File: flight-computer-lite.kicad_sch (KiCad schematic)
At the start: 44 parts, among them J1 USB_C_Receptacle_USB2.0_16P, J2 Micro_SD_Card_Det2, J3 Conn_01x02_Pin, J4 Conn_01x03_Pin, Q1 BSS138, SW1 SW_Push, SW2 SW_Push, U1 RP2040, U2 W25Q32JVZP, Y1 SiT1602BI-22-33E-12.000000E

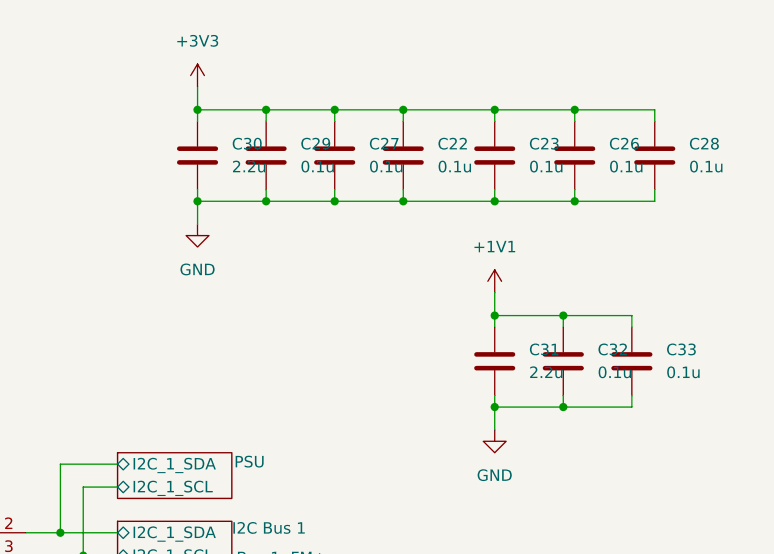
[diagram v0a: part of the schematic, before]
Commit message: Adjusted VREG IN/OUT Decoupling capacitor values to match datasheet suggestion
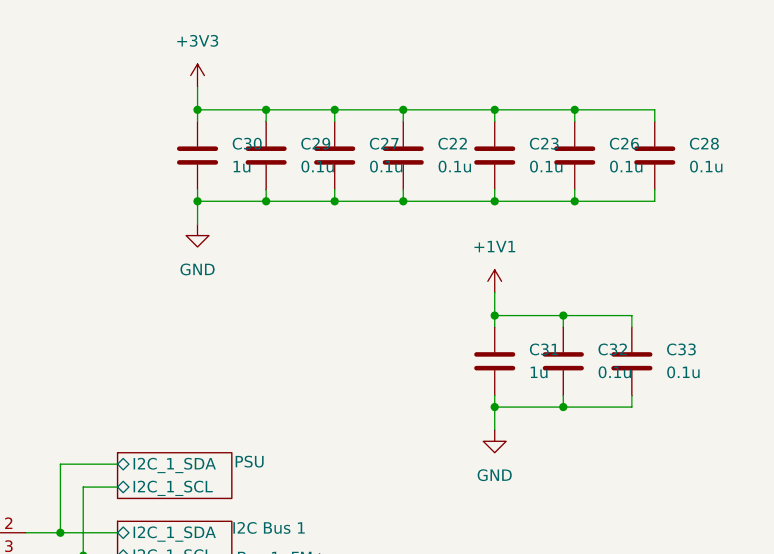
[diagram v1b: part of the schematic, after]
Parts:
- C30, C31: value 2.2u -> 1u
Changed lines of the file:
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@@
 			)
 		)
-		(property "Value" "2.2u"
+		(property "Value" "1u"
 			(at 255.27 54.6099 0)
 			(effects
@@
 			)
 		)
-		(property "Value" "2.2u"
+		(property "Value" "1u"
 			(at 222.25 31.7499 0)
 			(effects

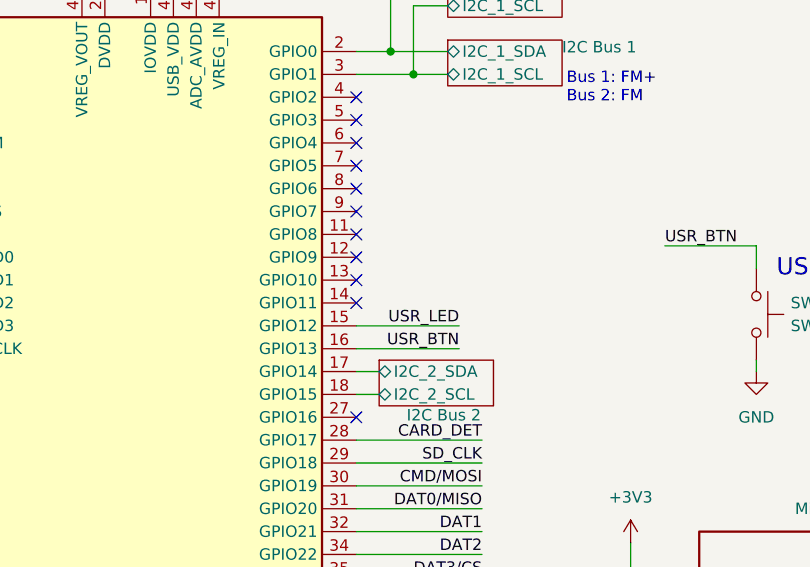
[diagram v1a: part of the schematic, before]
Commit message: Changed USR_LED and USR_BTN pins
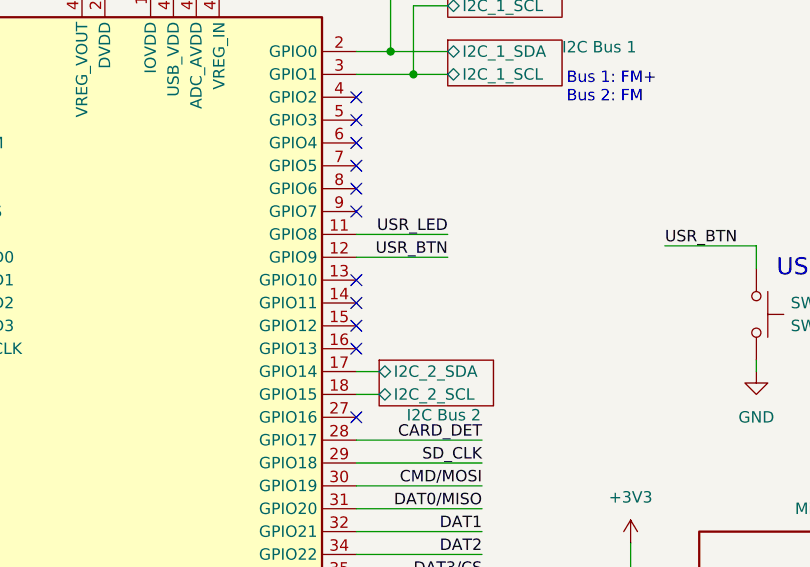
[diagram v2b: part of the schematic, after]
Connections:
- net USR_BTN: now also U1.12 (GPIO9); no longer U1.16 (GPIO13)
- net USR_LED: now also U1.11 (GPIO8); no longer U1.15 (GPIO12)
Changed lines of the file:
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@@
-	)
-	(no_connect
-		(at 199.39 95.25)
-	)
-	(no_connect
-		(at 199.39 92.71)
 	)
 	(no_connect
@@
 	)
 	(no_connect
+		(at 199.39 105.41)
+	)
+	(no_connect
 		(at 199.39 85.09)
 	)
@@
 	)
 	(no_connect
+		(at 199.39 102.87)
+	)
+	(no_connect
 		(at 199.39 100.33)
 	)
@@
 	(wire
 		(pts
+			(xy 199.39 92.71) (xy 209.55 92.71)
+		)
+		(stroke
+			(width 0)
+			(type default)
+		)
+	)
+	(wire
+		(pts
 			(xy 251.46 49.53) (xy 251.46 48.26)
 		)
@@
 	(wire
 		(pts
-			(xy 199.39 105.41) (xy 210.82 105.41)
-		)
-		(stroke
-			(width 0)
-			(type default)
-		)
-	)
-	(wire
-		(pts
 			(xy 205.74 67.31) (xy 205.74 74.93)
 		)
@@
 	(wire
 		(pts
+			(xy 199.39 95.25) (xy 209.55 95.25)
+		)
+		(stroke
+			(width 0)
+			(type default)
+		)
+	)
+	(wire
+		(pts
 			(xy 78.74 163.83) (xy 82.55 163.83)
 		)
@@
 		(pts
 			(xy 179.07 64.77) (xy 179.07 63.5)
-		)
-		(stroke
-			(width 0)
-			(type default)
-		)
-	)
-	(wire
-		(pts
-			(xy 199.39 102.87) (xy 210.82 102.87)
 		)
 		(stroke
@@
 	)
 	(label "USR_BTN"
-		(at 210.82 105.41 180)
+		(at 209.55 95.25 180)
 		(fields_autoplaced yes)
 		(effects
@@
 	)
 	(label "USR_LED"
-		(at 210.82 102.87 180)
-		(fields_autoplaced yes)
-		(effects
+		(at 209.55 92.71 180)
+		(fields_autoplaced yes)
+		(effects

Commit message: oops wrong pin again
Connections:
- net USR_BTN: now also U1.9 (GPIO7); no longer U1.12 (GPIO9)
- net USR_LED: now also U1.8 (GPIO6); no longer U1.11 (GPIO8)
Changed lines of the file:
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@@
+	)
+	(no_connect
+		(at 199.39 95.25)
+	)
+	(no_connect
+		(at 199.39 92.71)
 	)
 	(no_connect
@@
 	)
 	(no_connect
-		(at 199.39 87.63)
-	)
-	(no_connect
 		(at 52.07 107.95)
 	)
@@
 		(at 199.39 80.01)
 	)
-	(no_connect
-		(at 199.39 90.17)
-	)
 	(wire
 		(pts
@@
 	(wire
 		(pts
-			(xy 199.39 92.71) (xy 209.55 92.71)
-		)
-		(stroke
-			(width 0)
-			(type default)
-		)
-	)
-	(wire
-		(pts
 			(xy 251.46 49.53) (xy 251.46 48.26)
 		)
@@
 	(wire
 		(pts
+			(xy 199.39 90.17) (xy 209.55 90.17)
+		)
+		(stroke
+			(width 0)
+			(type default)
+		)
+	)
+	(wire
+		(pts
 			(xy 81.28 31.75) (xy 78.74 31.75)
 		)
@@
 	(wire
 		(pts
+			(xy 199.39 87.63) (xy 209.55 87.63)
+		)
+		(stroke
+			(width 0)
+			(type default)
+		)
+	)
+	(wire
+		(pts
 			(xy 270.51 83.82) (xy 270.51 85.09)
 		)
@@
 		(pts
 			(xy 78.74 44.45) (xy 78.74 45.72)
-		)
-		(stroke
-			(width 0)
-			(type default)
-		)
-	)
-	(wire
-		(pts
-			(xy 199.39 95.25) (xy 209.55 95.25)
 		)
 		(stroke
@@
 	)
 	(label "USR_BTN"
-		(at 209.55 95.25 180)
+		(at 209.55 90.17 180)
 		(fields_autoplaced yes)
 		(effects
@@
 	)
 	(label "USR_LED"
-		(at 209.55 92.71 180)
-		(fields_autoplaced yes)
-		(effects
+		(at 209.55 87.63 180)
+		(fields_autoplaced yes)
+		(effects

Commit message: WIP layout/route
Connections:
- net BUZZER_CTL: now also U1.7 (GPIO5)
- net I2C Bus 2/I2C_2_SCL: now also U1.14 (GPIO11); no longer U1.18 (GPIO15)
- net I2C Bus 2/I2C_2_SDA: now also U1.13 (GPIO10); no longer U1.17 (GPIO14)
- no-connect marks 18 -> 17
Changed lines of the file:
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@@
 	)
 	(no_connect
+		(at 199.39 110.49)
+	)
+	(no_connect
 		(at 199.39 95.25)
 	)
@@
 	)
 	(no_connect
-		(at 199.39 97.79)
+		(at 199.39 107.95)
 	)
 	(no_connect
@@
 	)
 	(no_connect
-		(at 199.39 85.09)
-	)
-	(no_connect
 		(at 199.39 135.89)
 	)
@@
 	)
 	(no_connect
-		(at 199.39 100.33)
-	)
-	(no_connect
 		(at 199.39 133.35)
 	)
@@
 	(wire
 		(pts
-			(xy 199.39 110.49) (xy 201.93 110.49)
-		)
-		(stroke
-			(width 0)
-			(type default)
-		)
-	)
-	(wire
-		(pts
 			(xy 199.39 118.11) (xy 213.36 118.11)
 		)
@@
 	(wire
 		(pts
+			(xy 199.39 100.33) (xy 201.93 100.33)
+		)
+		(stroke
+			(width 0)
+			(type default)
+		)
+	)
+	(wire
+		(pts
 			(xy 218.44 25.4) (xy 226.06 25.4)
 		)
@@
 	(wire
 		(pts
+			(xy 199.39 85.09) (xy 213.36 85.09)
+		)
+		(stroke
+			(width 0)
+			(type default)
+		)
+	)
+	(wire
+		(pts
 			(xy 146.05 148.59) (xy 148.59 148.59)
 		)
@@
 	(wire
 		(pts
-			(xy 199.39 107.95) (xy 201.93 107.95)
-		)
-		(stroke
-			(width 0)
-			(type default)
-		)
-	)
-	(wire
-		(pts
 			(xy 132.08 80.01) (xy 148.59 80.01)
 		)
@@
 	(wire
 		(pts
+			(xy 199.39 97.79) (xy 201.93 97.79)
+		)
+		(stroke
+			(width 0)
+			(type default)
+		)
+	)
+	(wire
+		(pts
 			(xy 137.16 102.87) (xy 148.59 102.87)
 		)
@@
 		)
 	)
+	(label "BUZZER_CTL"
+		(at 213.36 85.09 180)
+		(fields_autoplaced yes)
+		(effects
+			(font
+				(size 1.27 1.27)
+			)
+			(justify right bottom)
+		)
+	)
 	(label "QSPI_SD3"
 		(at 57.15 44.45 180)
@@
 	)
 	(sheet
-		(at 201.93 106.68)
+		(at 201.93 96.52)
 		(size 12.7 5.08)
 		(stroke
@@
 		)
 		(property "Sheetname" "I2C Bus 2"
-			(at 204.978 113.538 0)
+			(at 204.978 103.632 0)
 			(effects
 				(font
@@
 		)
 		(property "Sheetfile" "I2C_Bus_2.kicad_sch"
-			(at 201.93 111.0746 0)
+			(at 201.93 100.9146 0)
 			(effects
 				(font
@@
 		)
 		(pin "I2C_2_SCL" bidirectional
-			(at 201.93 110.49 180)
+			(at 201.93 100.33 180)
 			(effects
 				(font
@@
 		)
 		(pin "I2C_2_SDA" bidirectional
-			(at 201.93 107.95 180)
+			(at 201.93 97.79 180)
 			(effects
 				(font

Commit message: major routing update!
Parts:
- R11: value 1k -> 1K
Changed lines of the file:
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@@
 			)
 		)
-		(property "Value" "1k"
+		(property "Value" "1K"
 			(at 65.024 34.29 90)
 			(effects

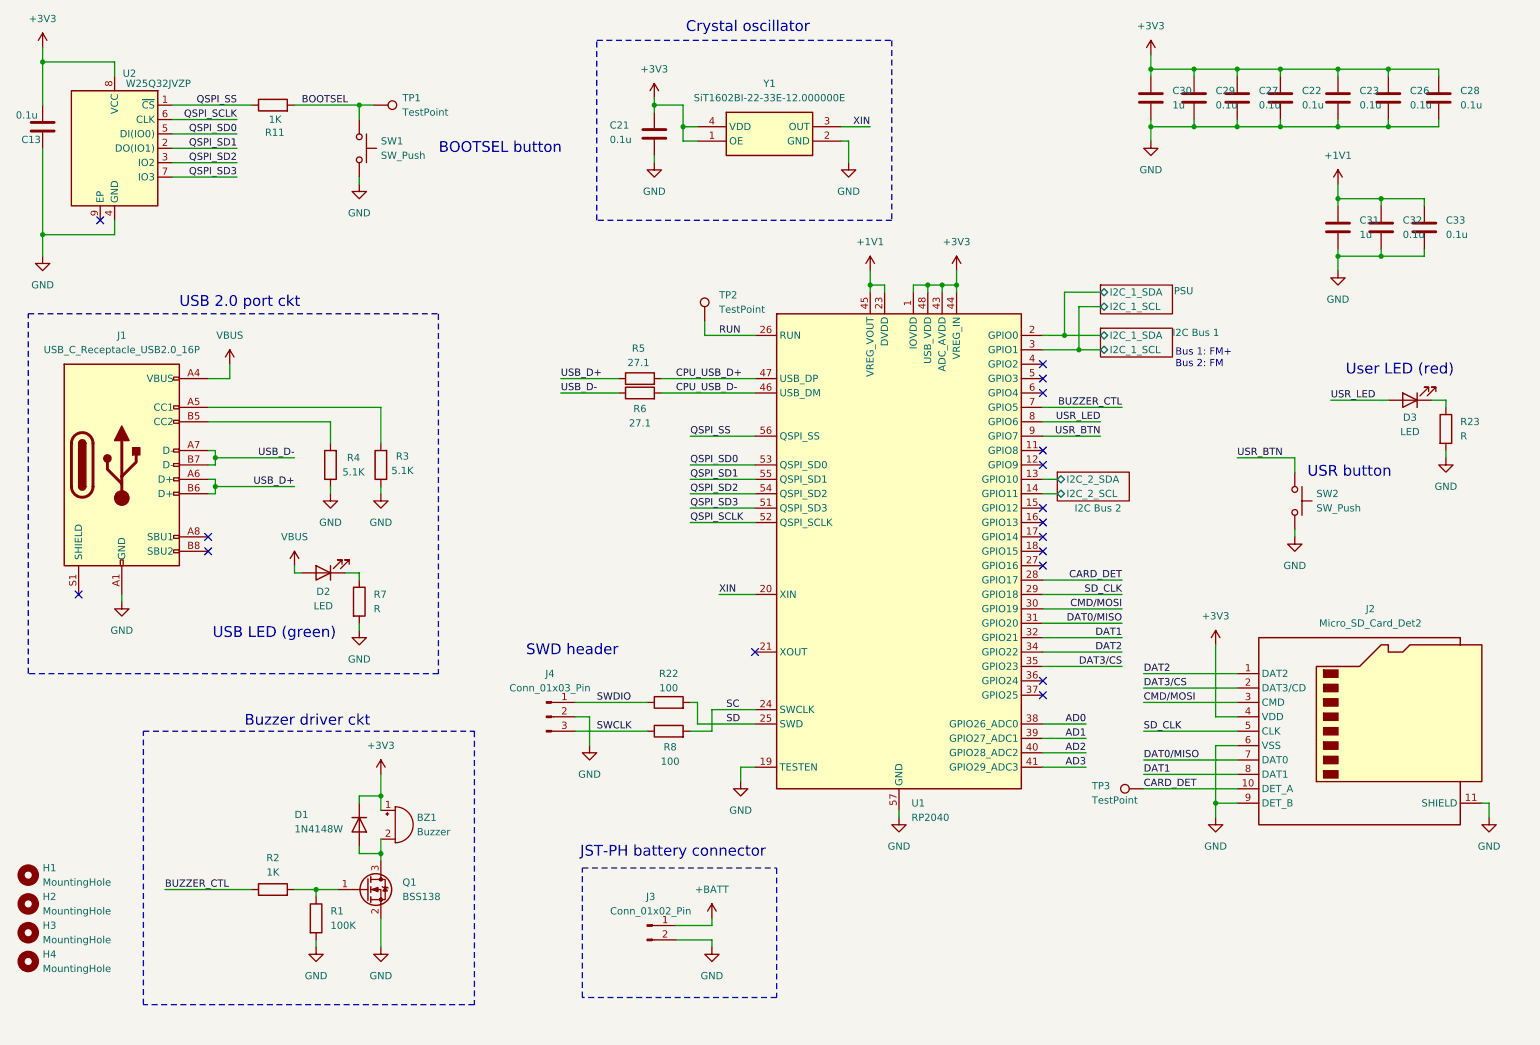
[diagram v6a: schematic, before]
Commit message: Fixed PSU, routed
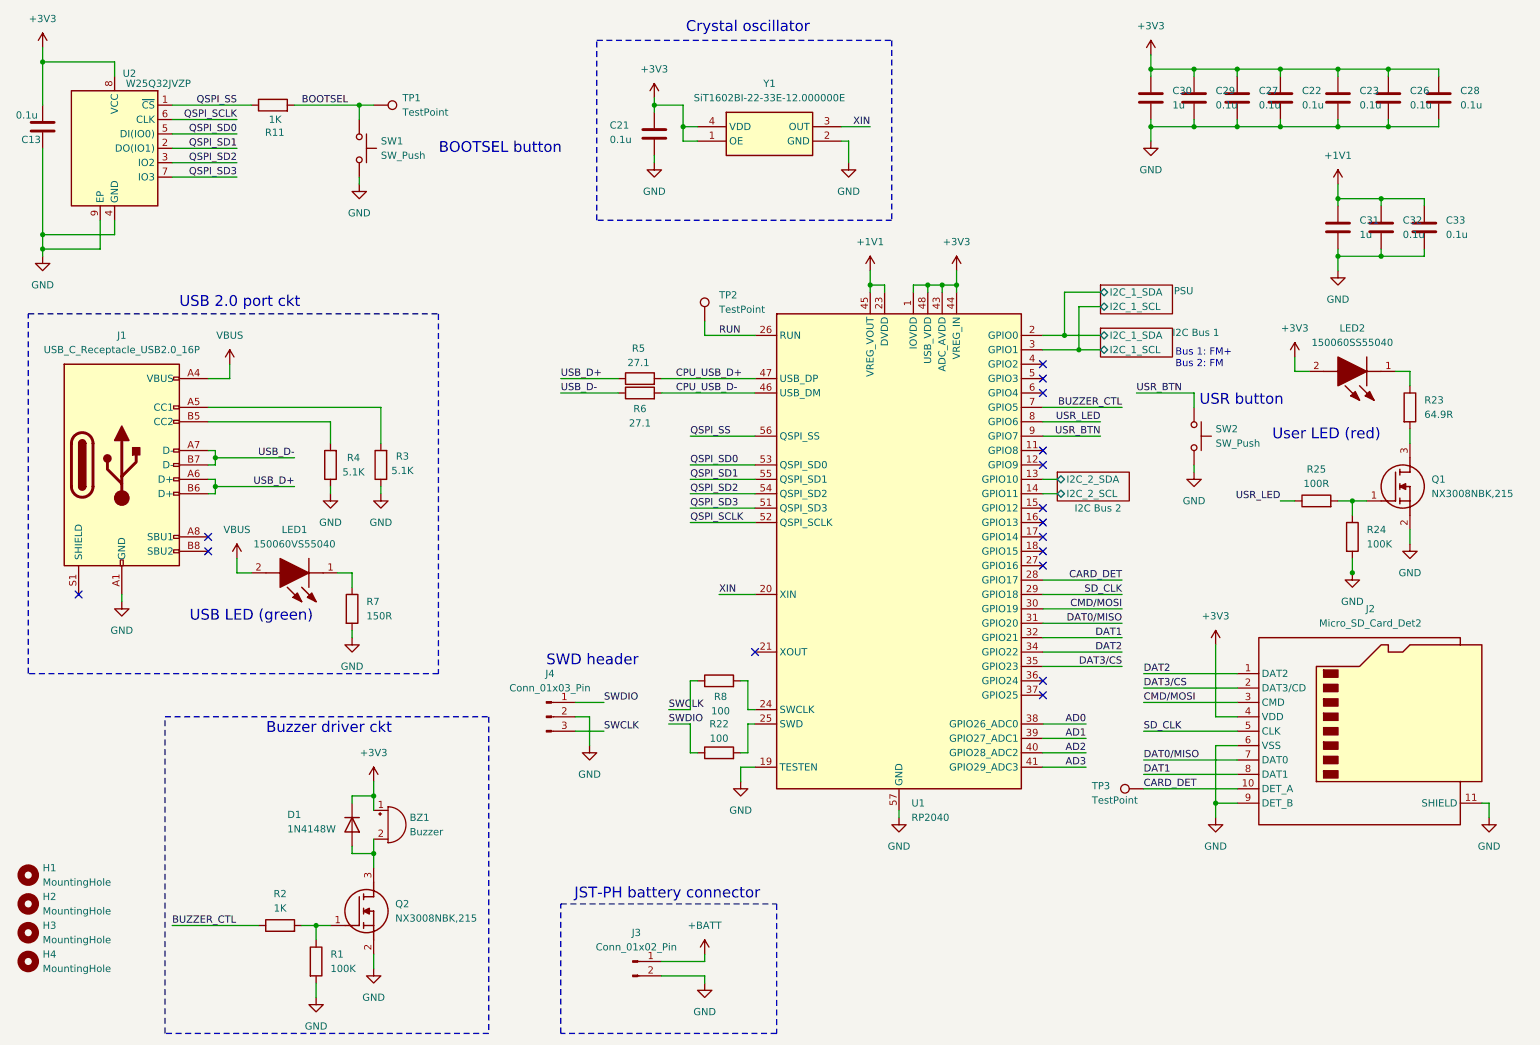
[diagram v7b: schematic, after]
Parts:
- removed D2, D3: LED, LED_SMD:LED_0603_1608Metric, symbol Device:LED
- removed Q1: BSS138, Package_TO_SOT_SMD:SOT-23, symbol Transistor_FET:BSS138
- added LED1: 150060VS55040, LEDM168X50N, symbol 150060VS55040:150060VS55040
- added LED2: 150060SS55040, 150060SS55040, symbol 150060SS55040:150060SS55040
- added Q1, Q2: NX3008NBK,215, NX3008NBK215, symbol NX3008NBK_215:NX3008NBK,215
- added R24: 100K, Resistor_SMD:R_0603_1608Metric, symbol Device:R
- added R25: 100R, Resistor_SMD:R_0603_1608Metric, symbol Device:R
- R23: value R -> 64.9R
- R7: value R -> 150R
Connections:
- net +3V3: now also LED2.2 (A)
- net GND: now also U2.9 (EP), Q1.2 (S), Q2.2 (S), R24.2; no longer R23.2
- net USR_LED: now also R25.1
- net VBUS: now also LED1.2 (A)
- net at R7.1: now also LED1.1 (K)
- net at R1.1, R2.2: now also Q2.1 (G)
- net at BZ1.2 (-), D1.2 (A): now also Q2.3 (D)
- net at R23.1: now also LED2.1 (K)
- net SC: no longer names the net of R8.2, U1.24 (SWCLK)
- net SD: no longer names the net of R22.2, U1.25 (SWD)
- new net: Q1.1 (G), R24.1, R25.2
- new net: Q1.3 (D), R23.2
- no-connect marks 17 -> 16
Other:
- moved on the sheet: BZ1, D1, J3, R1, R2, R22, R23, R7, R8, SW2
